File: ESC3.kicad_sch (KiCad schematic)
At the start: 35 parts, among them J11 SWD1, J12 MOTOR1, Q7 XRS306D, Q8 XRS306D, Q9 XRS306D, U12 STM32G071GBUxN, U13 DRV8300D

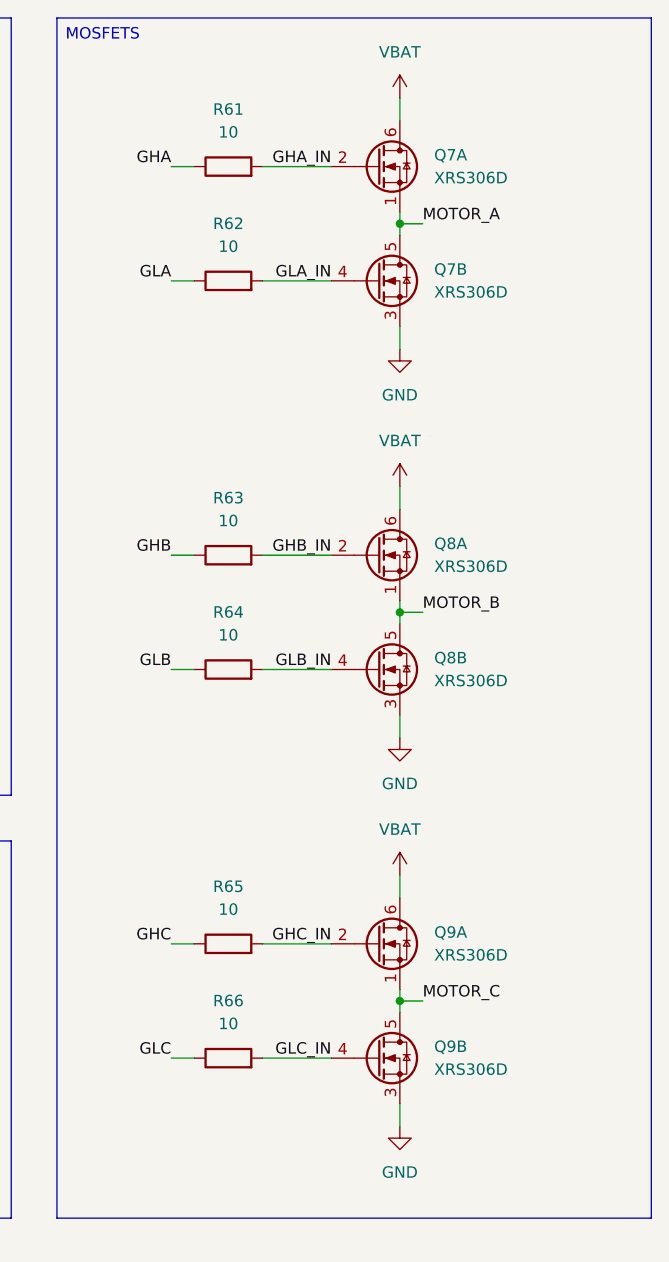
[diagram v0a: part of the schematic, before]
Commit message: License and ESC layout
Added a file extension to the license.
Updated the second ESC layout.

TODO:
Continue the ESC layout.
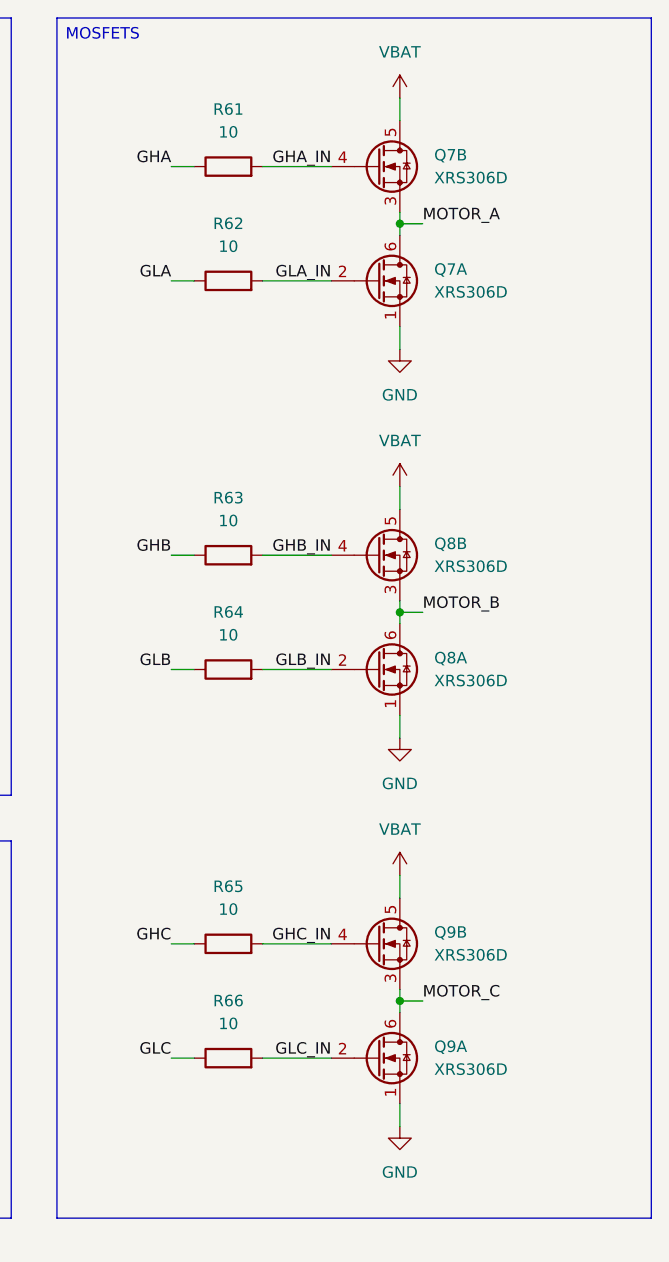
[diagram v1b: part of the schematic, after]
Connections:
- net GHA_IN: now also Q7.4 (G); no longer Q7.2 (G)
- net GHB_IN: now also Q8.4 (G); no longer Q8.2 (G)
- net GHC_IN: now also Q9.4 (G); no longer Q9.2 (G)
- net GLA_IN: now also Q7.2 (G); no longer Q7.4 (G)
- net GLB_IN: now also Q8.2 (G); no longer Q8.4 (G)
- net GLC_IN: now also Q9.2 (G); no longer Q9.4 (G)
- net GND: now also Q7.1 (S), Q8.1 (S), Q9.1 (S); no longer Q7.3 (S), Q8.3 (S), Q9.3 (S)
- net MOTOR_A: now also Q7.3 (S), Q7.6 (D); no longer Q7.1 (S), Q7.5 (D)
- net MOTOR_B: now also Q8.3 (S), Q8.6 (D); no longer Q8.1 (S), Q8.5 (D)
- net MOTOR_C: now also Q9.3 (S), Q9.6 (D); no longer Q9.1 (S), Q9.5 (D)
- net VBAT: now also Q7.5 (D), Q8.5 (D), Q9.5 (D); no longer Q7.6 (D), Q8.6 (D), Q9.6 (D)
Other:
- moved on the sheet: Q7A, Q7B, Q8A, Q8B, Q9A, Q9B

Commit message: ESC layout
Updated the layout for the final ESC.
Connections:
- net ESC3 renamed ESC2

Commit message: MCU layout
Updated the schematic labels.
Continued the MCU layout.
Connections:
- net ESC2 renamed ESC3
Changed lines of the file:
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@@
 		)
 	)
-	(global_label "ESC2"
+	(global_label "ESC3"
 		(shape input)
 		(at 107.95 64.77 0)

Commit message: Schematic revision
Added an ESP32 C3 for the ELRS receiver.
Updated the protection approach for the board.
Updated the net nodes.
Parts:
- removed C64, C65, C66, C67: 10u, Capacitor_SMD:C_1206_3216Metric, symbol Device:C
- added C59, C60, C62: 22u, Capacitor_SMD:C_1206_3216Metric, symbol Device:C
- C61, C63: value 10u -> 22u
- renumbered C60 to C57, C62 to C58, C68 to C64, C69 to C65, C70 to C66, C71 to C67, Q9 to Q10, Q7 to Q8, Q8 to Q9, R51 to R49, R52 to R50, R53 to R51, R54 to R52, R55 to R53, R56 to R54, R57 to R55, R58 to R56, R59 to R57, R60 to R58, R61 to R59, R62 to R60, R63 to R61, R64 to R62, R65 to R63, R66 to R64, U12 to U11, U13 to U12
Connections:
- net GND: now also C59.2, C60.2, C62.2
- net VBAT: now also C59.1, C60.1, C62.1

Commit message: IMU filtering and layout
Added a missing capacitor for the IMU.
Updated the PCB layout.
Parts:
- renumbered C57 to C52, C58 to C53, C59 to C54, C60 to C55, C61 to C56, C62 to C57, C63 to C58, C64 to C59, C65 to C60, C66 to C61, C67 to C62

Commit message: Oscillator and IMU layout
Updated the oscillator layout for the RP2350.
Updated the IMU layout for the IMU.
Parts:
- renumbered C52 to C53, C53 to C54, C54 to C55, C55 to C56, C56 to C57, C57 to C58, C58 to C59, C59 to C60, C60 to C61, C61 to C62, C62 to C63
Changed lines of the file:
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@@
 		(dnp no)
 		(fields_autoplaced yes)
-		(property "Reference" "C53"
+		(property "Reference" "C54"
 			(at 45.72 44.4499 0)
 			(effects
@@
 			(project "ThunderHorse"
 				(path "/ac187c6c-fa53-41cc-bce1-6f39a42a92e8/807a5f6f-4255-4cf0-8d90-acd62bb18590/f6401a6f-b04c-410e-81b5-25d3c51023df"
-					(reference "C53")
+					(reference "C54")
 					(unit 1)
 				)
@@
 		(dnp no)
 		(fields_autoplaced yes)
-		(property "Reference" "C60"
+		(property "Reference" "C61"
 			(at 184.15 44.45 90)
 			(effects
@@
 			(project "ThunderHorse"
 				(path "/ac187c6c-fa53-41cc-bce1-6f39a42a92e8/807a5f6f-4255-4cf0-8d90-acd62bb18590/f6401a6f-b04c-410e-81b5-25d3c51023df"
-					(reference "C60")
+					(reference "C61")
 					(unit 1)
 				)
@@
 		(dnp no)
 		(fields_autoplaced yes)
-		(property "Reference" "C59"
+		(property "Reference" "C60"
 			(at 144.78 40.6399 0)
 			(effects
@@
 			(project "ThunderHorse"
 				(path "/ac187c6c-fa53-41cc-bce1-6f39a42a92e8/807a5f6f-4255-4cf0-8d90-acd62bb18590/f6401a6f-b04c-410e-81b5-25d3c51023df"
-					(reference "C59")
+					(reference "C60")
 					(unit 1)
 				)
@@
 		(dnp no)
 		(fields_autoplaced yes)
-		(property "Reference" "C56"
+		(property "Reference" "C57"
 			(at 72.39 175.2599 0)
 			(effects
@@
 			(project "ThunderHorse"
 				(path "/ac187c6c-fa53-41cc-bce1-6f39a42a92e8/807a5f6f-4255-4cf0-8d90-acd62bb18590/f6401a6f-b04c-410e-81b5-25d3c51023df"
-					(reference "C56")
+					(reference "C57")
 					(unit 1)
 				)
@@
 		(dnp no)
 		(fields_autoplaced yes)
-		(property "Reference" "C61"
+		(property "Reference" "C62"
 			(at 184.15 58.42 90)
 			(effects
@@
 			(project "ThunderHorse"
 				(path "/ac187c6c-fa53-41cc-bce1-6f39a42a92e8/807a5f6f-4255-4cf0-8d90-acd62bb18590/f6401a6f-b04c-410e-81b5-25d3c51023df"
-					(reference "C61")
+					(reference "C62")
 					(unit 1)
 				)
@@
 		(dnp no)
 		(fields_autoplaced yes)
-		(property "Reference" "C62"
+		(property "Reference" "C63"
 			(at 184.15 72.39 90)
 			(effects
@@
 			(project "ThunderHorse"
 				(path "/ac187c6c-fa53-41cc-bce1-6f39a42a92e8/807a5f6f-4255-4cf0-8d90-acd62bb18590/f6401a6f-b04c-410e-81b5-25d3c51023df"
-					(reference "C62")
+					(reference "C63")
 					(unit 1)
 				)
@@
 		(dnp no)
 		(fields_autoplaced yes)
-		(property "Reference" "C58"
+		(property "Reference" "C59"
 			(at 97.79 175.2599 0)
 			(effects
@@
 			(project "ThunderHorse"
 				(path "/ac187c6c-fa53-41cc-bce1-6f39a42a92e8/807a5f6f-4255-4cf0-8d90-acd62bb18590/f6401a6f-b04c-410e-81b5-25d3c51023df"
-					(reference "C58")
+					(reference "C59")
 					(unit 1)
 				)
@@
 		(dnp no)
 		(fields_autoplaced yes)
-		(property "Reference" "C55"
+		(property "Reference" "C56"
 			(at 59.69 175.2599 0)
 			(effects
@@
 			(project "ThunderHorse"
 				(path "/ac187c6c-fa53-41cc-bce1-6f39a42a92e8/807a5f6f-4255-4cf0-8d90-acd62bb18590/f6401a6f-b04c-410e-81b5-25d3c51023df"
-					(reference "C55")
+					(reference "C56")
 					(unit 1)
 				)
@@
 		(on_board yes)
 		(dnp no)
-		(property "Reference" "C54"
+		(property "Reference" "C55"
 			(at 46.99 175.2599 0)
 			(effects
@@
 			(project "ThunderHorse"
 				(path "/ac187c6c-fa53-41cc-bce1-6f39a42a92e8/807a5f6f-4255-4cf0-8d90-acd62bb18590/f6401a6f-b04c-410e-81b5-25d3c51023df"
-					(reference "C54")
+					(reference "C55")
 					(unit 1)
 				)
@@
 		(dnp no)
 		(fields_autoplaced yes)
-		(property "Reference" "C57"
+		(property "Reference" "C58"
 			(at 85.09 175.2599 0)
 			(effects
@@
 			(project "ThunderHorse"
 				(path "/ac187c6c-fa53-41cc-bce1-6f39a42a92e8/807a5f6f-4255-4cf0-8d90-acd62bb18590/f6401a6f-b04c-410e-81b5-25d3c51023df"
-					(reference "C57")
+					(reference "C58")
 					(unit 1)
 				)
@@
 		(dnp no)
 		(fields_autoplaced yes)
-		(property "Reference" "C52"
+		(property "Reference" "C53"
 			(at 34.29 44.4499 0)
 			(effects
@@
 			(project "ThunderHorse"
 				(path "/ac187c6c-fa53-41cc-bce1-6f39a42a92e8/807a5f6f-4255-4cf0-8d90-acd62bb18590/f6401a6f-b04c-410e-81b5-25d3c51023df"
-					(reference "C52")
+					(reference "C53")
 					(unit 1)
 				)

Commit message: Power and ESC layout
Updated the power layout.
Updated the ESC layout.

TODO:
Improve track spacing for the ESC.
Complete the power connections.
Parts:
- C60: footprint Capacitor_SMD:C_0805_2012Metric -> Capacitor_SMD:C_0603_1608Metric
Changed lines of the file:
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@@
 			)
 		)
-		(property "Footprint" "Capacitor_SMD:C_0805_2012Metric"
+		(property "Footprint" "Capacitor_SMD:C_0603_1608Metric"
 			(at 141.9352 45.72 0)
 			(effects

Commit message: Voltage detection
Added a VBUS voltage detection for the RP.
Minor layout changes.
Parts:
- renumbered C60 to C53, C53 to C54, C54 to C55, C61 to C56, C62 to C57, C63 to C58, C55 to C59, C56 to C60, C57 to C61, C58 to C62, C59 to C63, R59 to R51, R60 to R52, R61 to R54, R62 to R55, R63 to R56, R50 to R57, R54 to R58, R57 to R59, R49 to R60, R52 to R61, R56 to R62, R64 to R63, R51 to R64, R55 to R65, R58 to R66
